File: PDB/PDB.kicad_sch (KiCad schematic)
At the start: 63 parts, among them J2 ESC - XT90x4, J3 FC - XT30x1, J4 Sensors - XT30x1, J5 Jetson - XT60x1, J6 UART OUT, J7 Micro_SD_Card, Q5 IPT012N08N5, Q6 BSC093N15NS5, Q7 IPT012N08N5, Q8 BSC093N15NS5, U10 LTC4359-DCB, U11 LTC4359-DCB, U13 MCP9804_DFN, U14 MCP9804_DFN, U15 MCP9804_DFN, U2 STM32H742VGTx

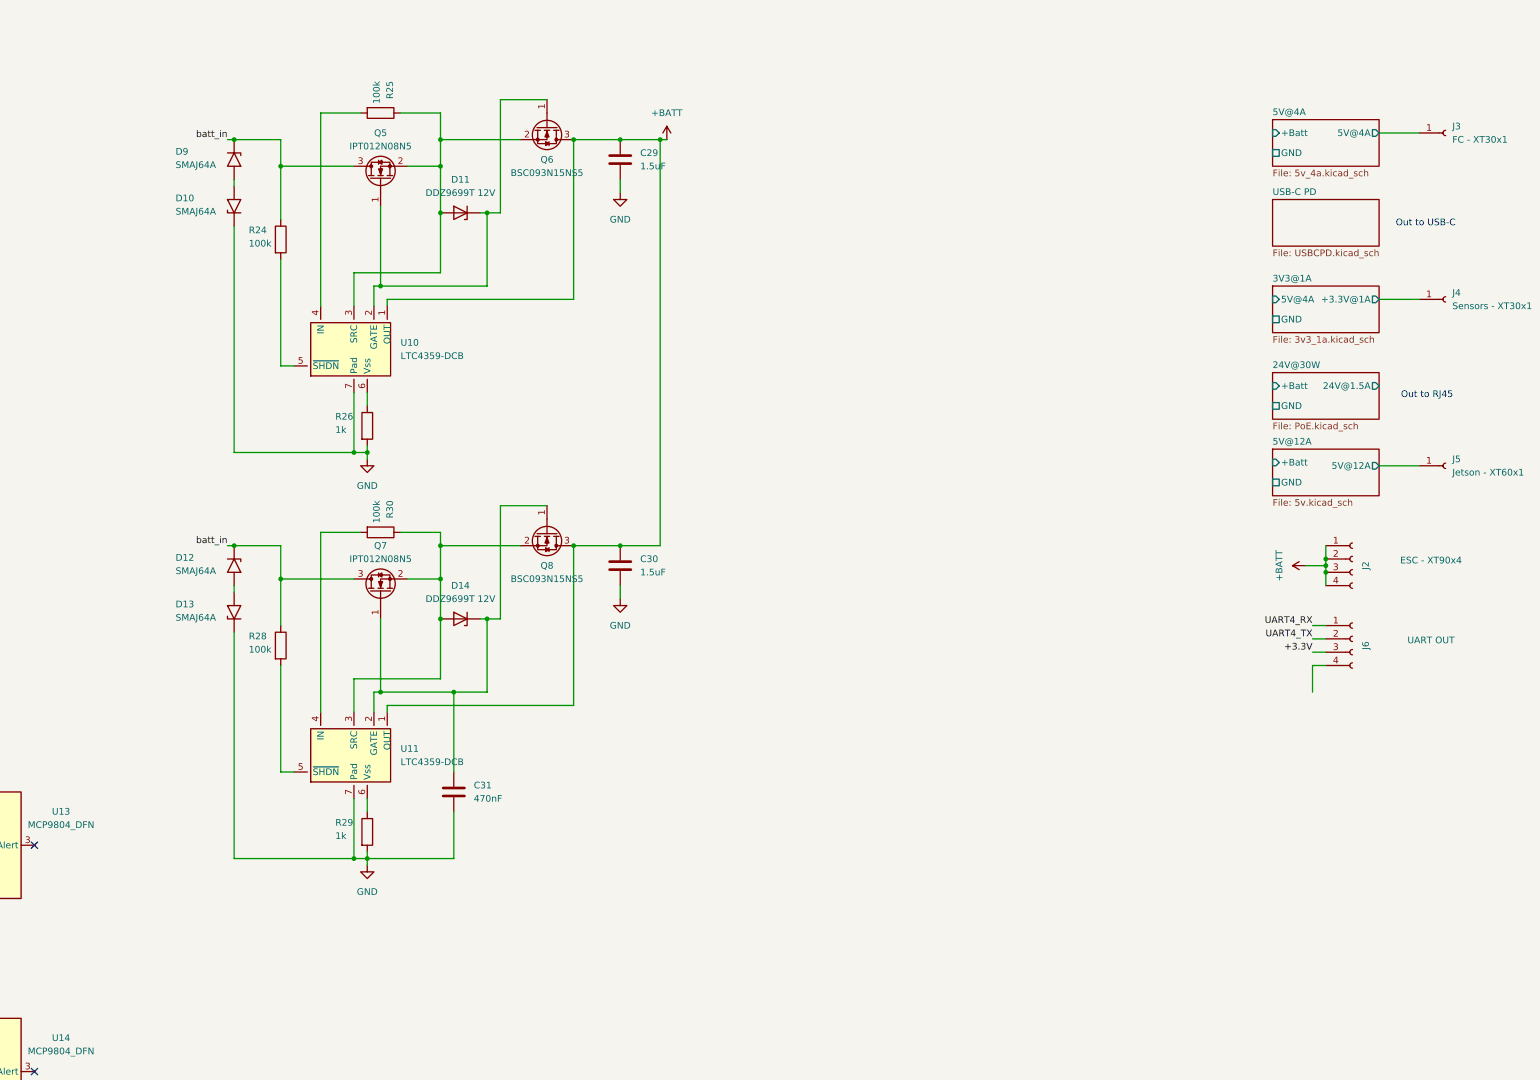
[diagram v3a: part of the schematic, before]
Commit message: added input current sense
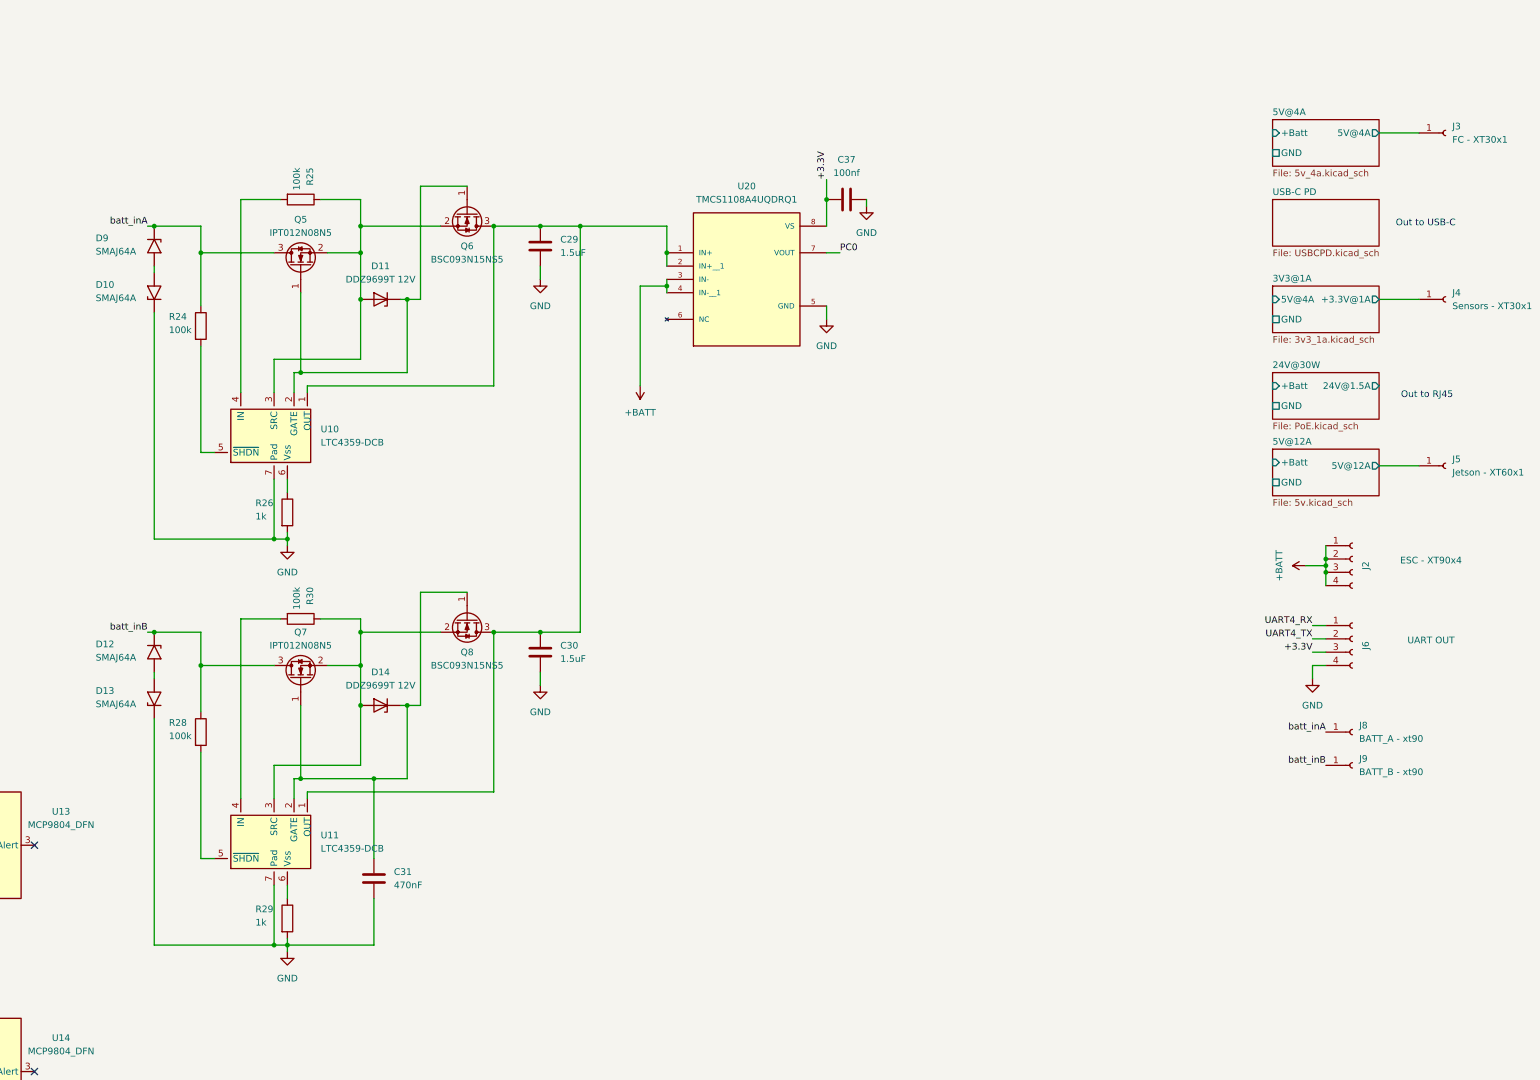
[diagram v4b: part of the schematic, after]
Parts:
- added C37: 100nf, Capacitor_SMD:C_1206_3216Metric, symbol Device:C
- added J8: BATT_A - xt90, symbol Connector:Conn_01x01_Socket
- added J9: BATT_B - xt90, symbol Connector:Conn_01x01_Socket
- added U20: TMCS1108A4UQDRQ1, TMCS1108A4UQDRQ1:SOIC127P599X175-8N, symbol sym&foot:TMCS1108A4UQDRQ1
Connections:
- net +3.3V: now also C37.1, U20.8 (VS)
- net +BATT: now also U20.3 (IN-), U20.4 (IN-__1); no longer C29.1, C30.1, Q6.3 (D), Q8.3 (D), U10.1 (OUT), U11.1 (OUT)
- net GND: now also J6.4 (Pin_4), C37.2, U20.5 (GND)
- net PC0: now also U20.7 (VOUT)
- net batt_in renamed batt_inA
- net batt_inA: now also J8.1 (Pin_1); no longer D12.1 (A1), Q7.3 (D), R28.1
- new net: C29.1, C30.1, Q6.3 (D), Q8.3 (D), U10.1 (OUT), U11.1 (OUT), U20.1 (IN+), U20.2 (IN+__1)
- new net batt_inB: D12.1 (A1), J9.1 (Pin_1), Q7.3 (D), R28.1
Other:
- moved on the sheet: C29, C30, C31, D10, D11, D12, D13, D14, D9, Q5, Q6, Q7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

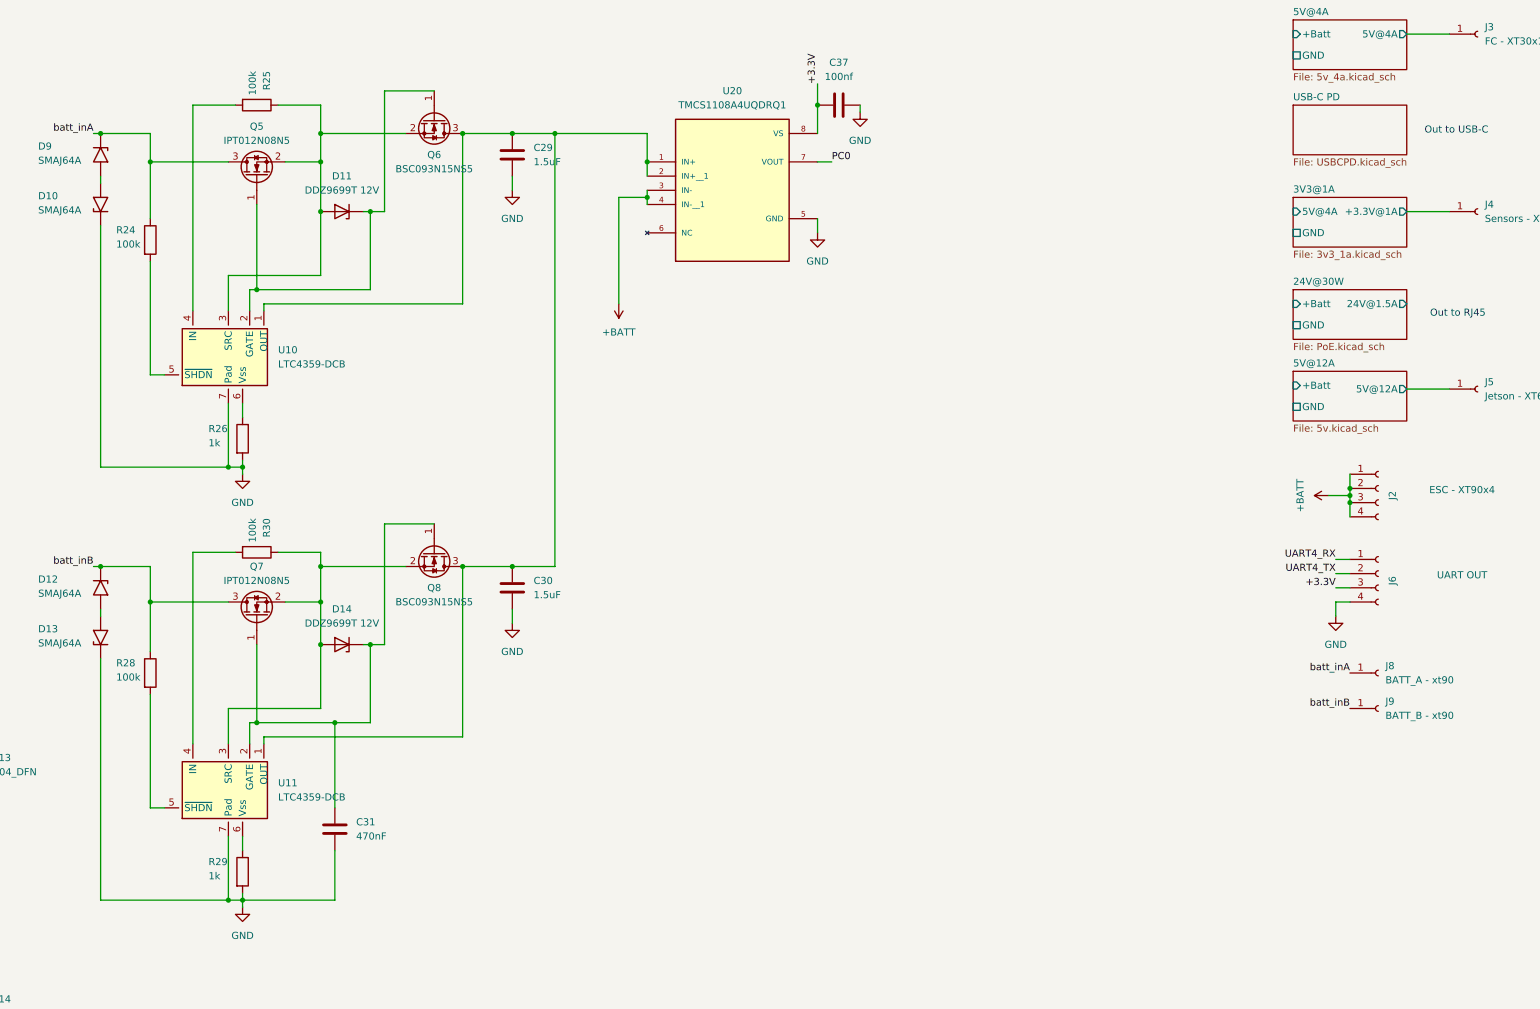
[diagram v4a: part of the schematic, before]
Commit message: added tp's, switches, inputs/outputs
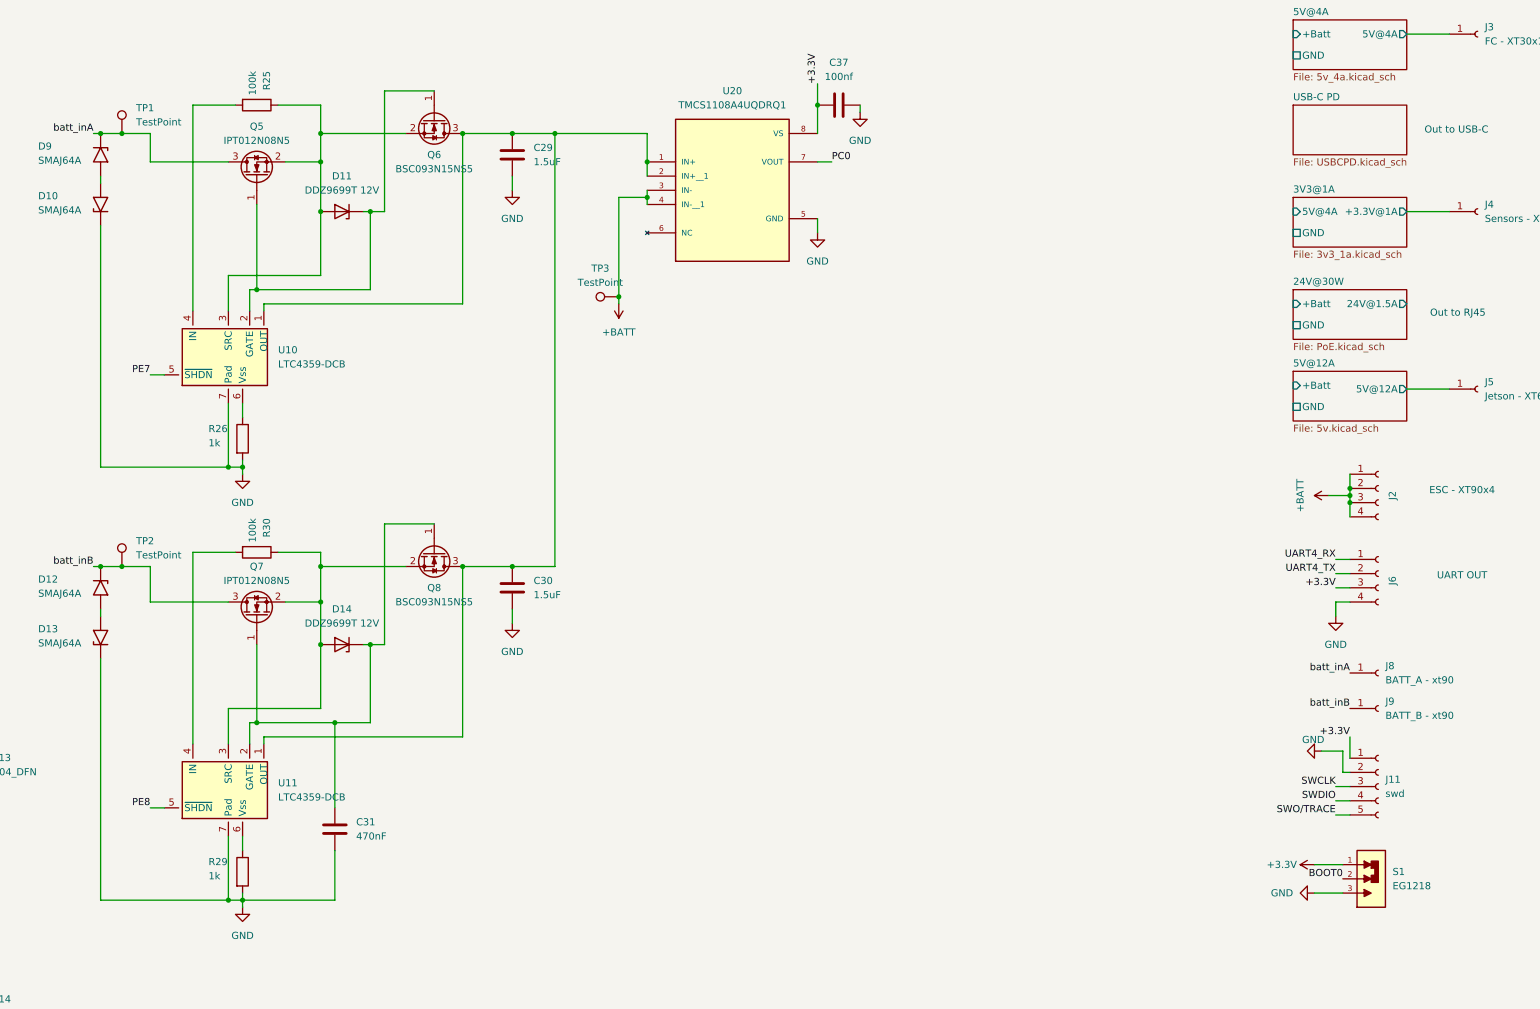
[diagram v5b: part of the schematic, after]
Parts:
- removed R24, R28: 100k, Resistor_SMD:R_0603_1608Metric_Pad0.98x0.95mm_HandSolder, symbol Device:R
- added J11: swd, symbol Connector:Conn_01x05_Socket
- added S1: EG1218, EG1218:SW_EG1218, symbol sym&foot:EG1218
- added TP1, TP2, TP3: TestPoint, TestPoint:TestPoint_Pad_D2.0mm, symbol Connector:TestPoint
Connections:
- net +3.3V: now also J11.1 (Pin_1), S1.1
- net +BATT: now also TP3.1
- net BOOT0: now also S1.2
- net GND: now also J11.2 (Pin_2), S1.3
- net PE7: now also U10.5 (~{SHDN})
- net PE8: now also U11.5 (~{SHDN})
- net SWCLK: now also J11.3 (Pin_3)
- net SWDIO: now also J11.4 (Pin_4)
- net SWO/TRACE: now also J11.5 (Pin_5)
- net batt_inA: now also TP1.1
- net batt_inB: now also TP2.1
